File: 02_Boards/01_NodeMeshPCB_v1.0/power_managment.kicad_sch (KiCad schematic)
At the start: 0 parts

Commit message: mppt solar charger schematic
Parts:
- added C10, C6: 10uF, symbol Device:C_Polarized
- added C11, C7: 4.7uF, symbol Device:C
- added C5: 220nF, symbol Device:C
- added C8: 470nF, symbol Device:C
- added C9: 100nF, symbol Device:C
- added D1: Red, symbol Device:LED
- added D2: Green, symbol Device:LED
- added D3, D4: RBR5LAM30ATFTR, symbol Device:D_Schottky
- added L1: 10uH, symbol Device:L
- added Q1: AOD4185, TO252_AOS, symbol AOD4185:AOD4185
- added R10, R9: R, symbol Device:R
- added R11: 10kOhm, symbol Device:R
- added R12, R8: 120Ohm, symbol Device:R
- added U3: CN3791, CN3791:SSOP-10-1MM, symbol CN3791:CN3791
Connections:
- new net: Q1.1 (G), U3.10 (DRV)
- new net: D3.2 (A), Q1.2 (D)
- new net: R8.1, U3.5 (COM)
- new net: C5.1, R8.2
- new net: D3.1 (K), D4.1 (K), L1.1
- new net: C9.1, U3.1 (VG)
- new net: D1.1 (K), U3.3 (~{CHRG})
- new net: D2.1 (K), U3.4 (~{DONE})
- new net: R10.1, R9.2, U3.6 (MPTT)
- new net: L1.2, R12.1, U3.8 (CSP)
- new net: D1.2 (A), D2.2 (A), R11.1
- new net BATT_CHARGE: C10.1, C11.1, R12.2, U3.7 (BAT)
- new net GND: C10.2, C11.2, C5.2, C6.2, C7.2, C8.2, D4.2 (A), R9.1, U3.2 (GND)
- new net SOLAR_IN: C6.1, C7.1, C8.1, C9.2, Q1.3 (S), R10.2, R11.2, U3.9 (VCC)
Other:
- note added: "CN3791 MPPT SOLAR CHARGER"

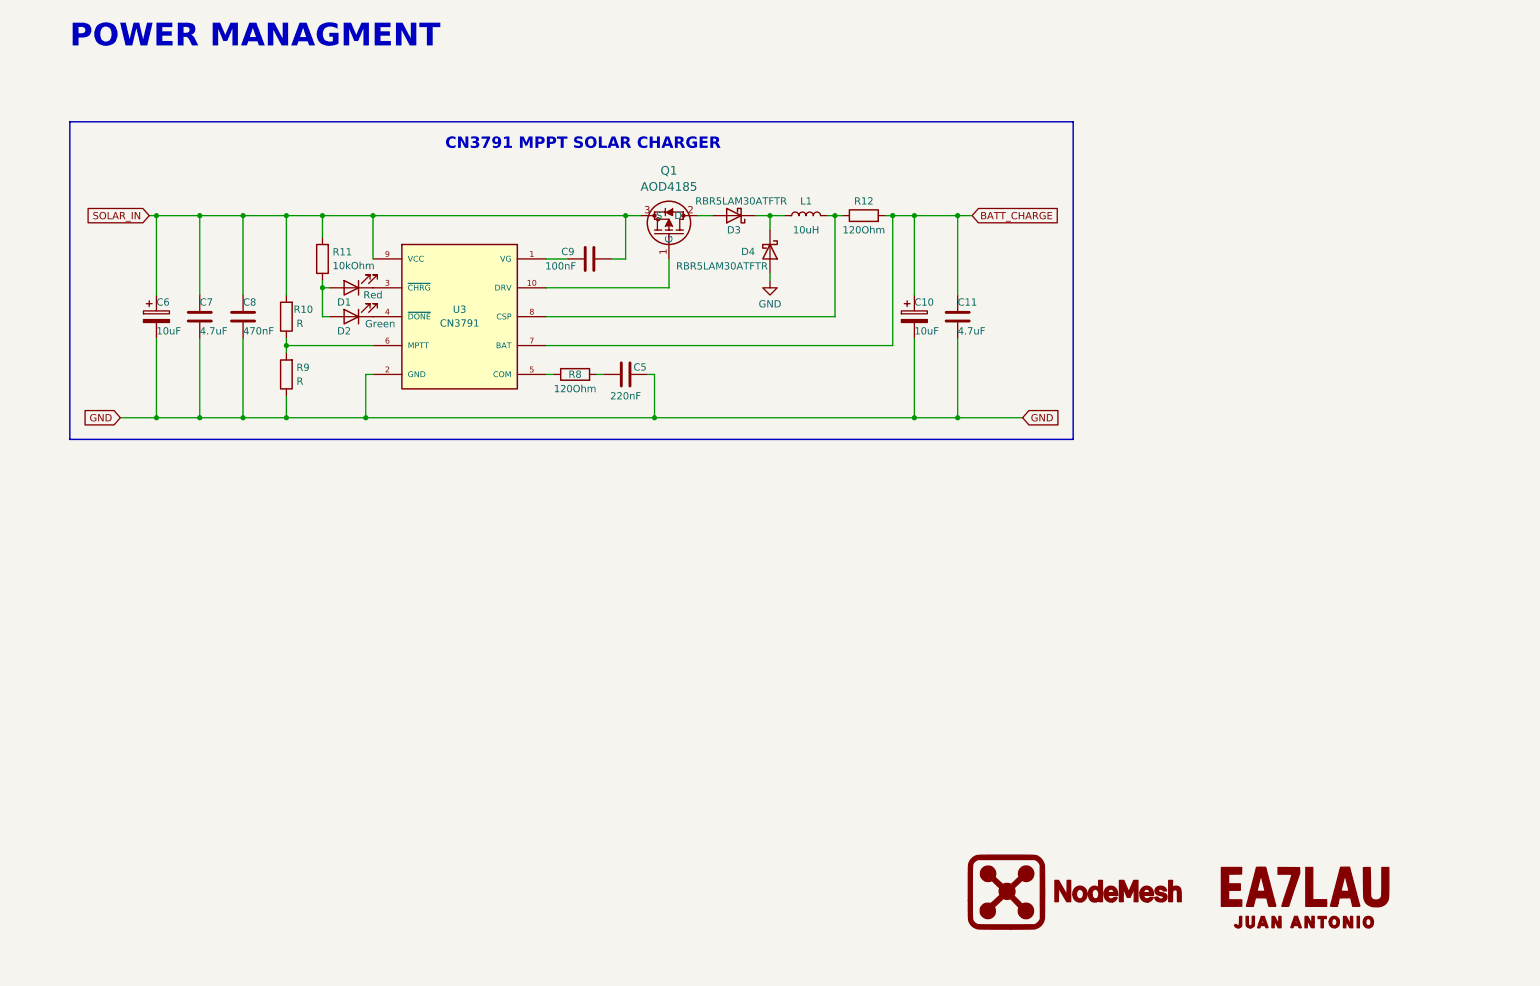
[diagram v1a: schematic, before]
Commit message: 3V3 LDO Schematic
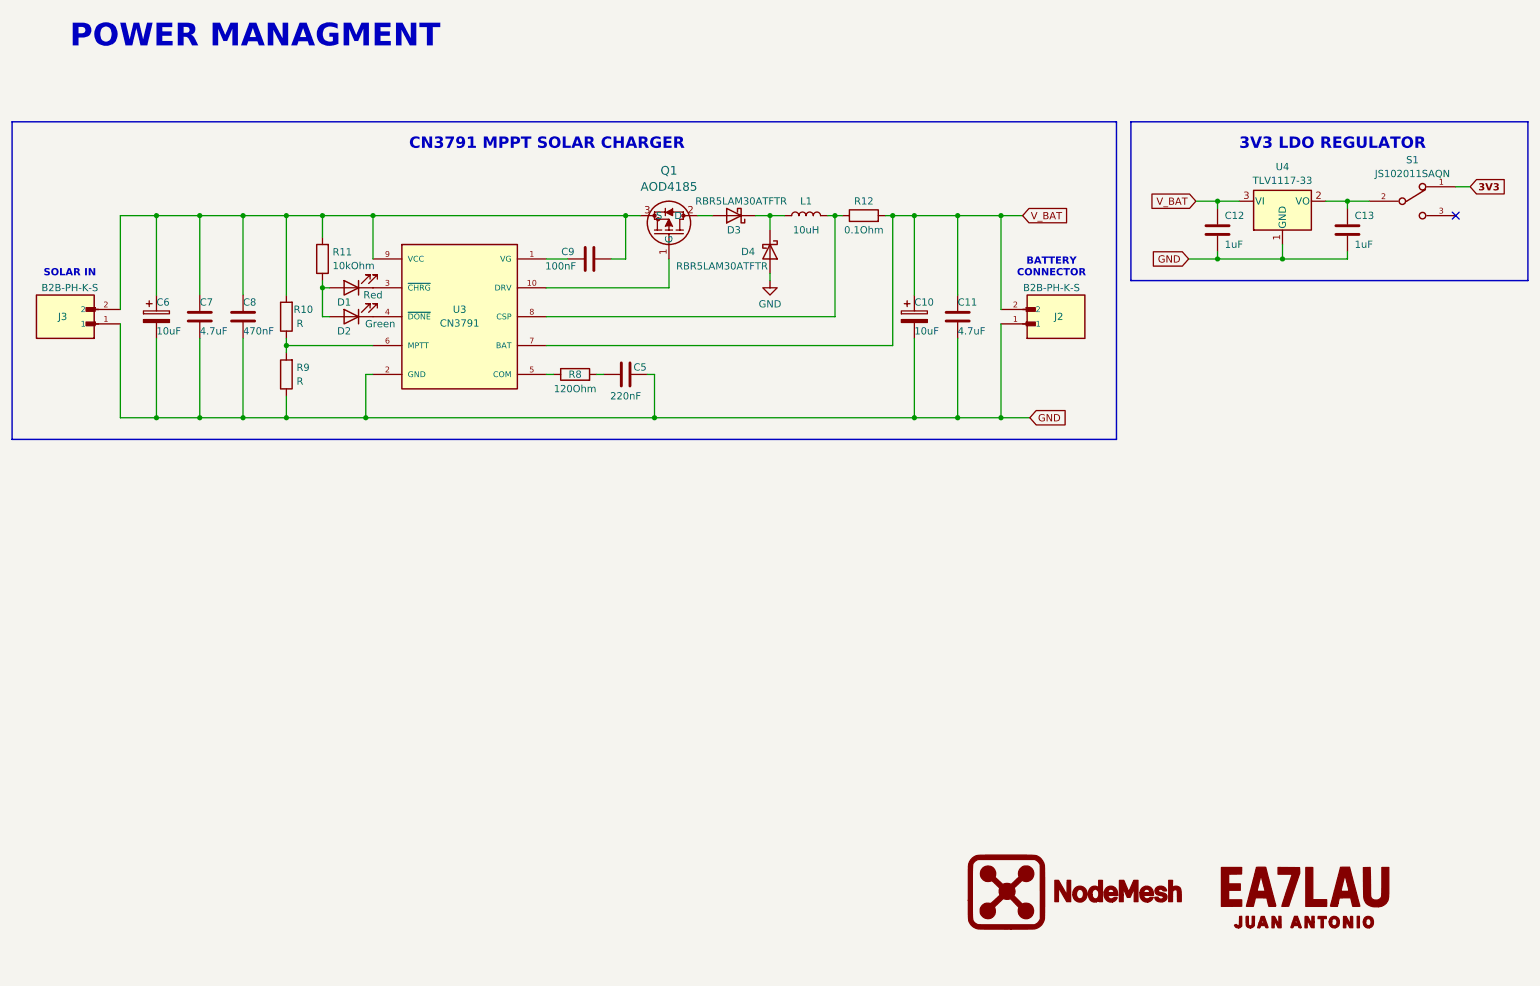
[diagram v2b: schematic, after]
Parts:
- added C12, C13: 1uF, symbol Device:C
- added J2, J3: B2B-PH-K-S, B2B-PH-K-S:JST_B2B-PH-K-S, symbol B2B-PH-K-S:B2B-PH-K-S
- added S1: JS102011SAQN, JS102011SAQN:SW_JS102011SAQN, symbol JS102011SAQN:JS102011SAQN
- added U4: TLV1117-33, symbol Regulator_Linear:TLV1117-33
- R12: value 120Ohm -> 0.1Ohm
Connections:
- net GND: now also C12.2, C13.2, J2.1, J3.1, U4.1 (GND)
- net BATT_CHARGE renamed V_BAT
- net V_BAT: now also C12.1, J2.2, U4.3 (VI)
- net SOLAR_IN: no longer names the net of C6.1, C7.1, C8.1, C9.2, Q1.3 (S), R10.2, R11.2, U3.9 (VCC)
- net SOLAR_IN: now also J3.2
- new net: C13.1, S1.2, U4.2 (VO)
- new net 3V3: S1.1
- no-connect marks 0 -> 1
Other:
- note added: "3V3 LDO REGULATOR"
- note added: "BATTERY CONNECTOR"
- note added: "SOLAR IN"

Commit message: Battery protection and measure schematics
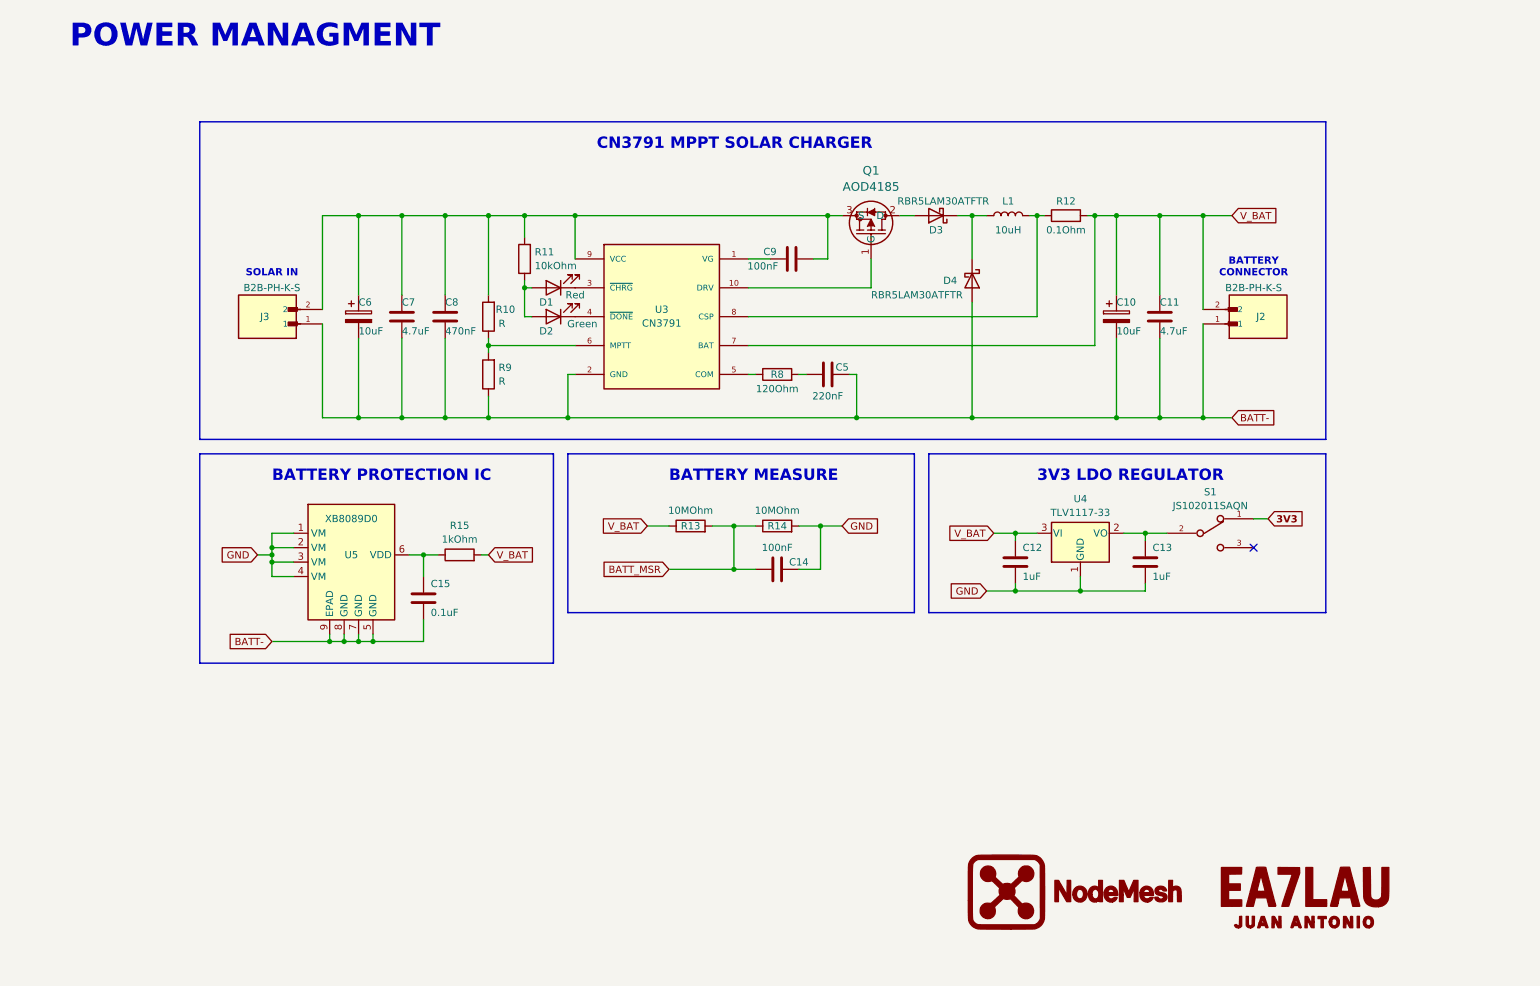
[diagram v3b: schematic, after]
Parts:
- added C14: 100nF, symbol Device:C
- added C15: 0.1uF, symbol Device:C
- added R13, R14: 10MOhm, symbol Device:R
- added R15: 1kOhm, symbol Device:R
- added U5: XB8089D0, Package_SO:SOIC-8-1EP_3.9x4.9mm_P1.27mm_EP2.41x3.3mm, symbol Regulator_Switching:LM25085MY
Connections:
- net GND: now also C14.2, R14.2, U5.1 (VM), U5.2 (VM), U5.3 (VM), U5.4 (VM); no longer C10.2, C11.2, C5.2, C6.2, C7.2, C8.2, D4.2 (A), J2.1, J3.1, R9.1, U3.2 (GND)
- net V_BAT: now also R13.1, R15.2
- new net: C15.1, R15.1, U5.6 (VDD)
- new net BATT-: C10.2, C11.2, C15.2, C5.2, C6.2, C7.2, C8.2, D4.2 (A), J2.1, J3.1, R9.1, U3.2 (GND), U5.5 (GND), U5.7 (GND), U5.8 (GND), U5.9 (EPAD)
- new net BATT_MSR: C14.1, R13.2, R14.1
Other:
- note added: "BATTERY MEASURE"
- note added: "BATTERY PROTECTION IC"
- moved on the sheet: C10, C11, C12, C13, C5, C6, C7, C8, C9, D1, D2, D3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

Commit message: Control Mosfets Shematic
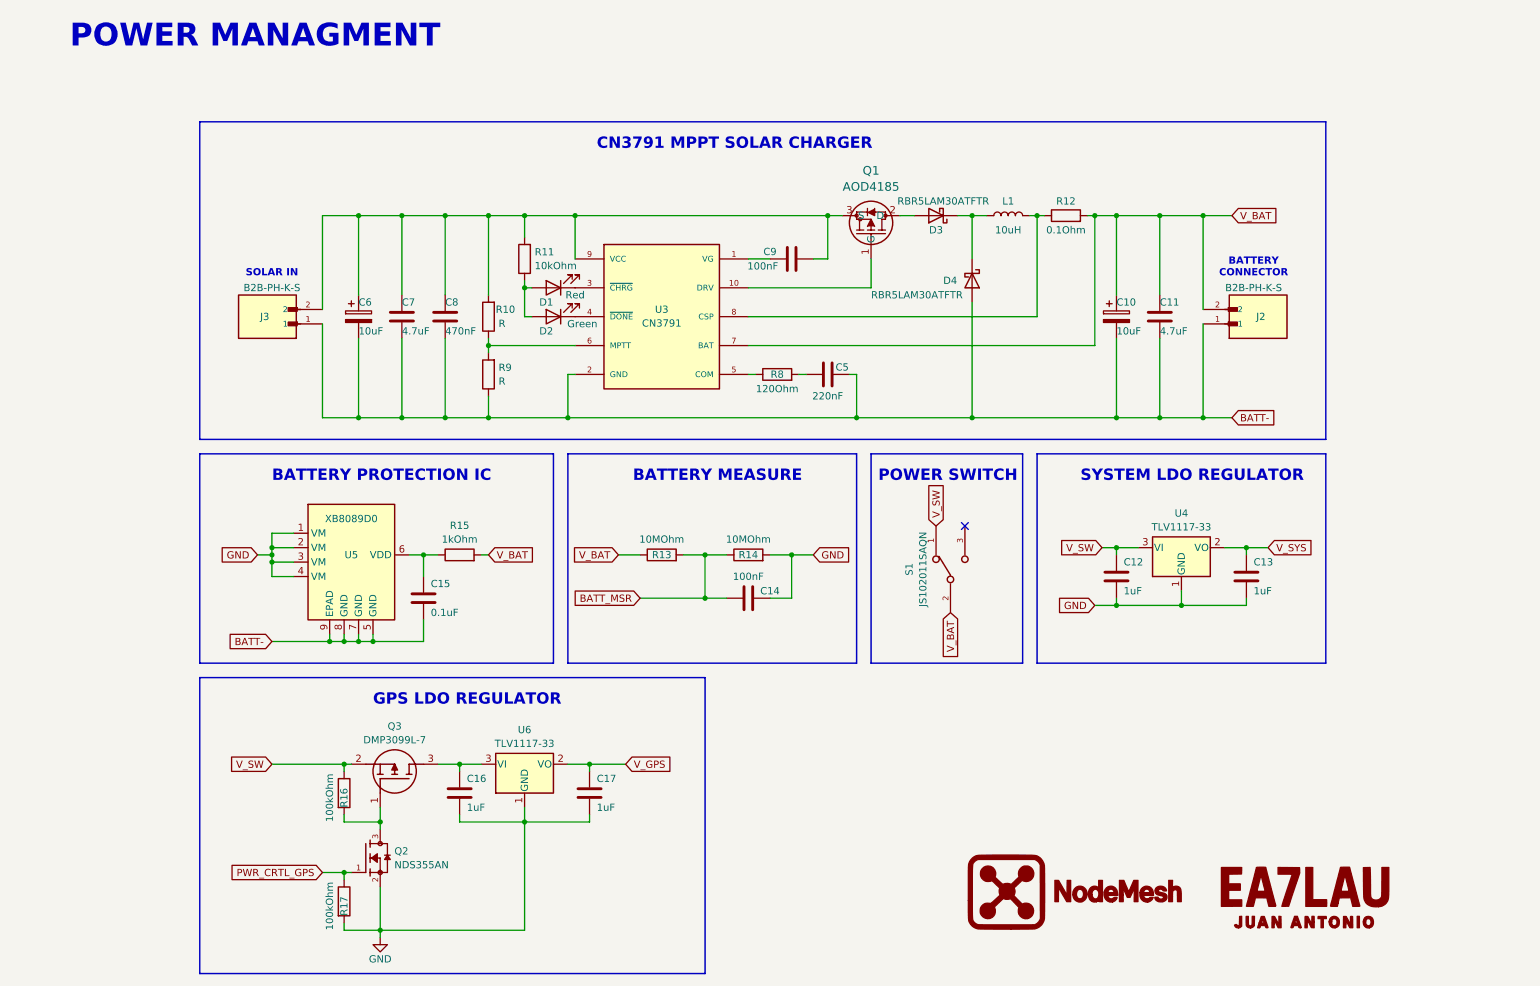
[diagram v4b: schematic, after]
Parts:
- added C16, C17: 1uF, symbol Device:C
- added Q2: NDS355AN, NDS355AN:SOT95P251X112-3N, symbol NDS355AN:NDS355AN
- added Q3: DMP3099L-7, SOT96P240X115-3N, symbol DMP3099L-7:DMP3099L-7
- added R16, R17: 100kOhm, symbol Device:R
- added U6: TLV1117-33, symbol Regulator_Linear:TLV1117-33
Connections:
- net GND: now also C16.2, C17.2, Q2.2, R17.2, U6.1 (GND)
- net V_BAT: now also S1.2; no longer C12.1, U4.3 (VI)
- net V_SYS: now reaches C13.1, U4.2 (VO)
- net V_SYS: no longer S1.2
- net 3V3 renamed V_SW
- net V_SW: now also C12.1, U4.3 (VI), Q3.2 (S), R16.1
- new net: Q2.3, Q3.1 (G), R16.2
- new net: C16.1, Q3.3 (D), U6.3 (VI)
- new net PWR_CRTL_GPS: Q2.1, R17.1
- new net V_GPS: C17.1, U6.2 (VO)
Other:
- note added: "GPS LDO REGULATOR"
- note added: "POWER SWITCH"
- note added: "SYSTEM LDO REGULATOR"
- note removed: "3V3 LDO REGULATOR"
- moved on the sheet: C12, C13, C14, R13, R14, S1, U4

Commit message: ht-ra62 schematic
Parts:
- removed C14: 100nF, symbol Device:C
- removed R13, R14: 10MOhm, symbol Device:R
- renumbered C6 to C1, C13 to C12, C7 to C2, C8 to C3, C15 to C4, C16 to C5, C17 to C6, C9 to C7, C5 to C8, C12 to C9, J3 to J1, Q3 to Q1, Q1 to Q3, R16 to R1, R17 to R2, R10 to R3, R9 to R4, R15 to R5, R11 to R6, R8 to R7, R12 to R8, U5 to U1, U6 to U2
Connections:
- net INA_CH3-: now reaches C1.1, C2.1, C3.1, C7.2, Q3.3 (S), R3.2, R6.2, U3.9 (VCC)
- net INA_CH3-: no longer J1.2
- net V_BAT renamed INA_CH2+
- net INA_CH2+: no longer J2.2, R5.2, S1.2
- new net INA_CH1+: J2.2
- new net INA_CH1-: R5.2, S1.2
- new net INA_CH3+: J1.2
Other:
- note removed: "BATTERY MEASURE"
- moved on the sheet: C12, C4, C9, J1, R5, S1, U1, U4

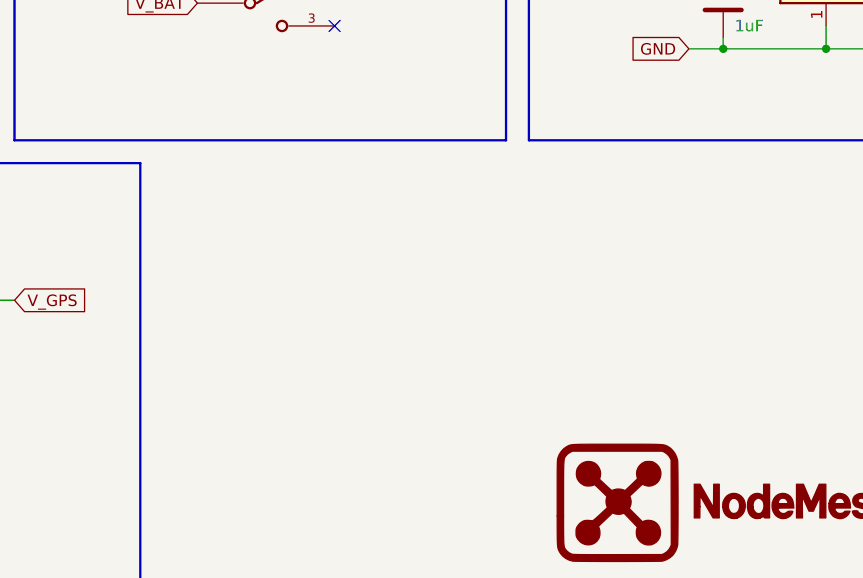
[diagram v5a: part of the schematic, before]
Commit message: nRF52840 schematic
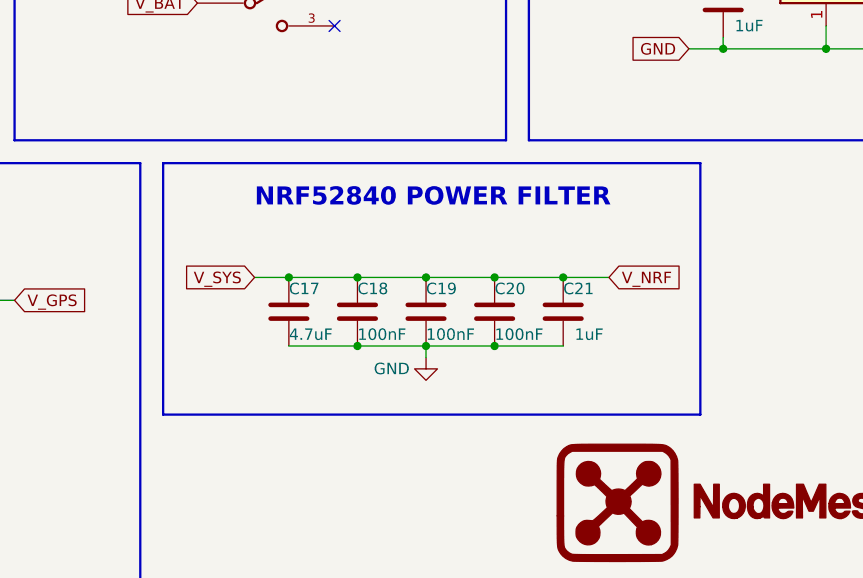
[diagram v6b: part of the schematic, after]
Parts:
- added C17: 4.7uF, symbol Device:C
- added C18, C19, C20: 100nF, symbol Device:C
- added C21: 1uF, symbol Device:C
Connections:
- net GND: now also C17.2, C18.2, C19.2, C20.2, C21.2
- net V_SYS renamed V_NRF
- net V_NRF: now also C17.1, C18.1, C19.1, C20.1, C21.1
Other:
- note added: "NRF52840 POWER FILTER"

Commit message: PCB placement
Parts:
- added C18: 10uF, Capacitor_SMD:C_0603_1608Metric, symbol Device:C
- added C19: 100nF, Capacitor_SMD:C_0603_1608Metric, symbol Device:C
- added C20: 33pF, Capacitor_SMD:C_0603_1608Metric, symbol Device:C
- C1: renamed from C7; footprint (none) -> Capacitor_SMD:C_0603_1608Metric
- C10: renamed from C4; footprint (none) -> Capacitor_SMD:C_0603_1608Metric
- C11: renamed from C17; footprint (none) -> Capacitor_SMD:C_0603_1608Metric
- C12: renamed from C18; footprint (none) -> Capacitor_SMD:C_0603_1608Metric
- C13: renamed from C19; footprint (none) -> Capacitor_SMD:C_0603_1608Metric
- C14: renamed from C20; footprint (none) -> Capacitor_SMD:C_0603_1608Metric
- C15: renamed from C21; footprint (none) -> Capacitor_SMD:C_0603_1608Metric
- C16: renamed from C5; footprint (none) -> Capacitor_SMD:C_0603_1608Metric
- C17: renamed from C6; footprint (none) -> Capacitor_SMD:C_0603_1608Metric
- C2: renamed from C1; footprint (none) -> Capacitor_SMD:C_0603_1608Metric
- C3: renamed from C2; footprint (none) -> Capacitor_SMD:C_0603_1608Metric
- C4: renamed from C3; footprint (none) -> Capacitor_SMD:C_0603_1608Metric
- C5: renamed from C10; footprint (none) -> Capacitor_SMD:C_0603_1608Metric
- C6: renamed from C11; footprint (none) -> Capacitor_SMD:C_0603_1608Metric
- C7: renamed from C8; footprint (none) -> Capacitor_SMD:C_0603_1608Metric
- C8: renamed from C9; footprint (none) -> Capacitor_SMD:C_0603_1608Metric
- C9: renamed from C12; footprint (none) -> Capacitor_SMD:C_0603_1608Metric
- D1: renamed from D3; footprint (none) -> 01_Footprints:RBR5LAM30ATFTR
- D2: renamed from D4; footprint (none) -> 01_Footprints:RBR5LAM30ATFTR
- D3: renamed from D1; footprint (none) -> LED_SMD:LED_0603_1608Metric
- D4: renamed from D2; footprint (none) -> LED_SMD:LED_0603_1608Metric
- J1, J2: value B2B-PH-K-S -> 1751248; footprint B2B-PH-K-S:JST_B2B-PH-K-S -> TerminalBlock_Phoenix:TerminalBlock_Phoenix_MKDS-1,5-2-5.08_1x02_P5.08mm_Horizontal
- L1: footprint (none) -> Inductor_SMD:L_0603_1608Metric
- Q1: renamed from Q3; footprint TO252_AOS -> 01_Footprints:AOD4185
- Q2: renamed from Q1; footprint SOT96P240X115-3N -> 01_Footprints:DMP3099L-7
- Q3: renamed from Q2; footprint NDS355AN:SOT95P251X112-3N -> 01_Footprints:NDS355AN
- R1: renamed from R8; footprint (none) -> Resistor_SMD:R_1206_3216Metric
- R2: renamed from R6; footprint (none) -> Resistor_SMD:R_0603_1608Metric
- R3: value R -> 178kOhm; footprint (none) -> Resistor_SMD:R_0603_1608Metric
- R4: value R -> 22kOhm; footprint (none) -> Resistor_SMD:R_0603_1608Metric
- R5: renamed from R7; footprint (none) -> Resistor_SMD:R_0603_1608Metric
- R6: renamed from R5; footprint (none) -> Resistor_SMD:R_0603_1608Metric
- R7: renamed from R1; footprint (none) -> Resistor_SMD:R_0603_1608Metric
- R8: renamed from R2; footprint (none) -> Resistor_SMD:R_0603_1608Metric
- S1: footprint JS102011SAQN:SW_JS102011SAQN -> 01_Footprints:JS102011SAQN
- U1: renamed from U3; footprint CN3791:SSOP-10-1MM -> 01_Footprints:CN3791
- U2: renamed from U4; footprint (none) -> 01_Footprints:TLV1117LV33DCYR
- U3: renamed from U1; footprint Package_SO:SOIC-8-1EP_3.9x4.9mm_P1.27mm_EP2.41x3.3mm -> 01_Footprints:XB8089D0
- U4: renamed from U2; footprint (none) -> 01_Footprints:TLV1117LV33DCYR
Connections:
- net GND: now also C18.2, C19.2, C20.2
- net V_GPS: now also C18.1, C19.1, C20.1
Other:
- moved on the sheet: C11, C12, C13, C14, C15
